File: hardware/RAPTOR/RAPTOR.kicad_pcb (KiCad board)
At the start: 2 copper layers, 68.6 x 53.3 mm, 12 parts, among them P1 Power, P2 Analog, P3 Digital, P4 Digital, P5 CONN_01X01, P6 CONN_01X01, P7 CONN_01X01, P8 CONN_01X01

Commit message: add net + pcb files
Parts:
- moved REF** 86.4 mm to (114.8, 109.9), turned to 90 degrees
- moved REF** 85.2 mm to (114.8, 87.0), turned to 90 degrees
- moved REF** 58.8 mm to (172.0, 107.3), turned to 270 degrees
- moved REF** 49.7 mm to (172.0, 84.5), turned to 270 degrees

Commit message: put stuff on pcb thing
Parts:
- removed REF**: BNO055, RAPTOR_footprints:BNO055
- removed REF**: OpenLog, RAPTOR_footprints:OpenLog
- removed REF**: BMP280, RAPTOR_footprints:BMP280
- removed REF**: Adafruit GPS, RAPTOR_footprints:AdafruitGPS
- added BZ1: Buzzer, Buzzer_Beeper:Buzzer_12x9.5RM7.6, F.Cu at (126.2, 88.3)
- added D8: DIODE-1N4148, Silicon-Custom:DIODE-1N4148, F.Cu at (179.6, 38.7)
- added D9: DIODE-1N4148, Silicon-Custom:DIODE-1N4148, F.Cu at (199.6, 59.0)
- added J1: SOLC_CONN, Connectors:1X02, F.Cu at (257.0, 42.5)
- added J10: EXT_LED3, Connectors:1X02, F.Cu at (229.1, 46.4)
- added J11: SRVOL_CONN, Connectors:1X03, F.Cu at (150.4, 41.3)
- added J12: SRVOR_CONN, Connectors:1X03, F.Cu at (210.1, 75.6)
- added J13: HOTWIRE_CONN, Connectors:1X02, F.Cu at (196.1, 40.0)
- added J14: RBF_CONN, Connectors:1X03, F.Cu at (165.6, 48.9)
- added J15: EEPROM_BTN_CONN, Connectors:1X02, F.Cu at (216.4, 45.1)
- added J16: SOLC_SW_CONN, Connectors:1X03, F.Cu at (232.9, 76.8)
- added J17: SOLP_SW_CONN, Connectors:1X03, F.Cu at (177.0, 57.8)
- added J2: SOLP_CONN, Connectors:1X02, F.Cu at (216.4, 19.7)
- added J4: CONN_LED_FIX, Connectors:1X02, F.Cu at (218.9, 65.4)
- added J5: CONN_SOLP_LED, Connectors:1X02, F.Cu at (222.8, 55.2)
- added J6: CONN_SOLC_LED, Connectors:1X02, F.Cu at (248.2, 73.0)
- added J7: EXT_LED0, Connectors:1X02, F.Cu at (259.6, 66.7)
- added J8: EXT_LED1, Connectors:1X02, F.Cu at (221.5, 84.5)
- added J9: EXT_LED2, Connectors:1X02, F.Cu at (229.1, 59.1)
- added Q1: MOSFET-NCH-2N7002PW, Silicon-Standard:TO-92, F.Cu at (210.1, 33.7)
- added Q2: MOSFET-NCH-2N7002PW, Silicon-Standard:TO-92, F.Cu at (246.9, 32.4)
- added Q3: MOSFET-NCH-2N7002PW, Silicon-Standard:TO-92, F.Cu at (236.7, 67.9)
- added Q4: MOSFET-NCH-2N7002PW, Silicon-Standard:TO-92, F.Cu at (227.8, 18.4)
- added Q5: MOSFET-NCH-2N7002PW, Silicon-Standard:TO-92, F.Cu at (250.7, 54.0)
- added R1: 20OHM-0603-1_10W-1%, Resistor_THT:R_Axial_DIN0204_L3.6mm_D1.6mm_P5.08mm_Horizontal, F.Cu at (238.0, 23.5)
- added R2: 100OHM-0603-1_10W-1%, Resistor_THT:R_Axial_DIN0204_L3.6mm_D1.6mm_P5.08mm_Horizontal, F.Cu at (271.0, 48.9)
- added R3: 100OHM-0603-1_10W-1%, Resistor_THT:R_Axial_DIN0204_L3.6mm_D1.6mm_P5.08mm_Horizontal, F.Cu at (268.5, 31.1)
- added R4: 100OHM-0603-1_10W-1%, Resistor_THT:R_Axial_DIN0204_L3.6mm_D1.6mm_P5.08mm_Horizontal, F.Cu at (268.5, 78.1)
- added R5: 4.7KOHM-0603-1_10W-1%, Resistor_THT:R_Axial_DIN0204_L3.6mm_D1.6mm_P5.08mm_Horizontal, F.Cu at (257.0, 15.9)
- added R6: 4.7KOHM-0603-1_10W-1%, Resistor_THT:R_Axial_DIN0204_L3.6mm_D1.6mm_P5.08mm_Horizontal, F.Cu at (248.2, 87.0)
- added R7: 4.7KOHM-0603-1_10W-1%, Resistor_THT:R_Axial_DIN0204_L3.6mm_D1.6mm_P5.08mm_Horizontal, F.Cu at (205.0, 50.2)
- added R8: 4.7KOHM-0603-1_10W-1%, Resistor_THT:R_Axial_DIN0204_L3.6mm_D1.6mm_P5.08mm_Horizontal, F.Cu at (192.3, 32.4)
- added U1: BMP280 Breakout, RAPTOR_footprints:BMP280, F.Cu at (154.2, 90.8)
- added U2: BNO055 Breakout, RAPTOR_footprints:BNO055, F.Cu at (137.7, 120.0)
- added U3: OpenLog, RAPTOR_footprints:OpenLog, F.Cu at (113.5, 89.5)
- added U4: AdafruitGPS, RAPTOR_footprints:AdafruitGPS, F.Cu at (175.8, 103.5)
- added U5: U3V12F12, RAPTOR_footprints:U3V12F12, F.Cu at (112.3, 109.9)
- added U6: D24V550F5, RAPTOR_footprints:D24v50f5_Reg, F.Cu at (113.5, 123.8)
- moved P8 2.84 mm to (175.8, 88.3)
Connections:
- P2 pad 1: /A0 -> (no net)
- P2 pad 2: /A1 -> (no net)
- P2 pad 3: /A2 -> (no net)
- P2 pad 4: /A3 -> (no net)
- P2 pad 5: /A4(SDA) -> (no net)
- P2 pad 6: /A5(SCL) -> (no net)
- P3 pad 1: /A5(SCL) -> (no net)
- P3 pad 10: /8 -> (no net)
- P3 pad 2: /A4(SDA) -> (no net)
- P3 pad 3: /AREF -> (no net)
- P3 pad 4: GND -> (no net)
- P3 pad 5: /13(SCK) -> (no net)
- P3 pad 6: /12(MISO) -> (no net)
- P3 pad 7: /11(**/MOSI) -> (no net)
- P3 pad 8: /10(**/SS) -> /SOLC_DTA
- P3 pad 9: /9(**) -> (no net)
- P4 pad 1: /7 -> (no net)
- P4 pad 2: /6(**) -> /GPS_RX
- P4 pad 3: /5(**) -> (no net)
- P4 pad 4: /4 -> /HOTWIRE
- P4 pad 5: /3(**) -> (no net)
- P4 pad 6: /2 -> (no net)
- P4 pad 7: /1(Tx) -> /EEPROM_BTN
- P4 pad 8: /0(Rx) -> (no net)

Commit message: extend board
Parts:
- moved U4 39.4 mm to (215.1, 103.0)
- moved P8 1.98 mm to (177.0, 89.8)
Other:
- board size 68.6 x 53.3 mm -> 88.9 x 53.3 mm
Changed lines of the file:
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@@
   (general
     (thickness 1.6)
-    (drawings 27)
+    (drawings 24)
     (tracks 0)
     (zones 0)
@@
   )
   (module Socket_Arduino_Uno:Arduino_1pin locked (layer F.Cu)
-    (at 175.768 88.265)
+    (at 177.038 89.789)
     (descr "module 1 pin (ou trou mecanique de percage)")
     (tags DEV)
@@
   )
   (module RAPTOR_footprints:AdafruitGPS (layer F.Cu)
-    (at 175.768 103.505 270)
+    (at 215.138 102.997 270)
     (descr "A footprint for the Adafruit GPS Breakout Board")
     (fp_text reference U4 (at 0 3.81 270) (layer F.SilkS)
@@
     )
   )
+  (gr_line (start 199.898 73.025) (end 175.514 73.025) (layer Edge.Cuts) (width 0.15))
+  (gr_line (start 199.898 126.365) (end 199.898 73.025) (layer Edge.Cuts) (width 0.15))
+  (gr_line (start 177.038 126.365) (end 199.898 126.365) (layer Edge.Cuts) (width 0.15))
   (gr_text 1 (at 138.938 121.285 90) (layer F.SilkS)
     (effects (font (size 1 1) (thickness 0.15)))
@@
   (gr_line (start 114.427 74.93) (end 120.269 74.93) (angle 90) (layer Dwgs.User) (width 0.15))
   (gr_line (start 120.523 93.98) (end 104.648 93.98) (angle 90) (layer Dwgs.User) (width 0.15))
-  (gr_line (start 177.038 74.549) (end 175.514 73.025) (angle 90) (layer Edge.Cuts) (width 0.15))
-  (gr_line (start 177.038 85.979) (end 177.038 74.549) (angle 90) (layer Edge.Cuts) (width 0.15))
-  (gr_line (start 179.578 88.519) (end 177.038 85.979) (angle 90) (layer Edge.Cuts) (width 0.15))
-  (gr_line (start 179.578 121.285) (end 179.578 88.519) (angle 90) (layer Edge.Cuts) (width 0.15))
-  (gr_line (start 177.038 123.825) (end 179.578 121.285) (angle 90) (layer Edge.Cuts) (width 0.15))
-  (gr_line (start 177.038 126.365) (end 177.038 123.825) (angle 90) (layer Edge.Cuts) (width 0.15))
   (gr_line (start 110.998 126.365) (end 177.038 126.365) (angle 90) (layer Edge.Cuts) (width 0.15))
   (gr_line (start 110.998 73.025) (end 110.998 126.365) (angle 90) (layer Edge.Cuts) (width 0.15))

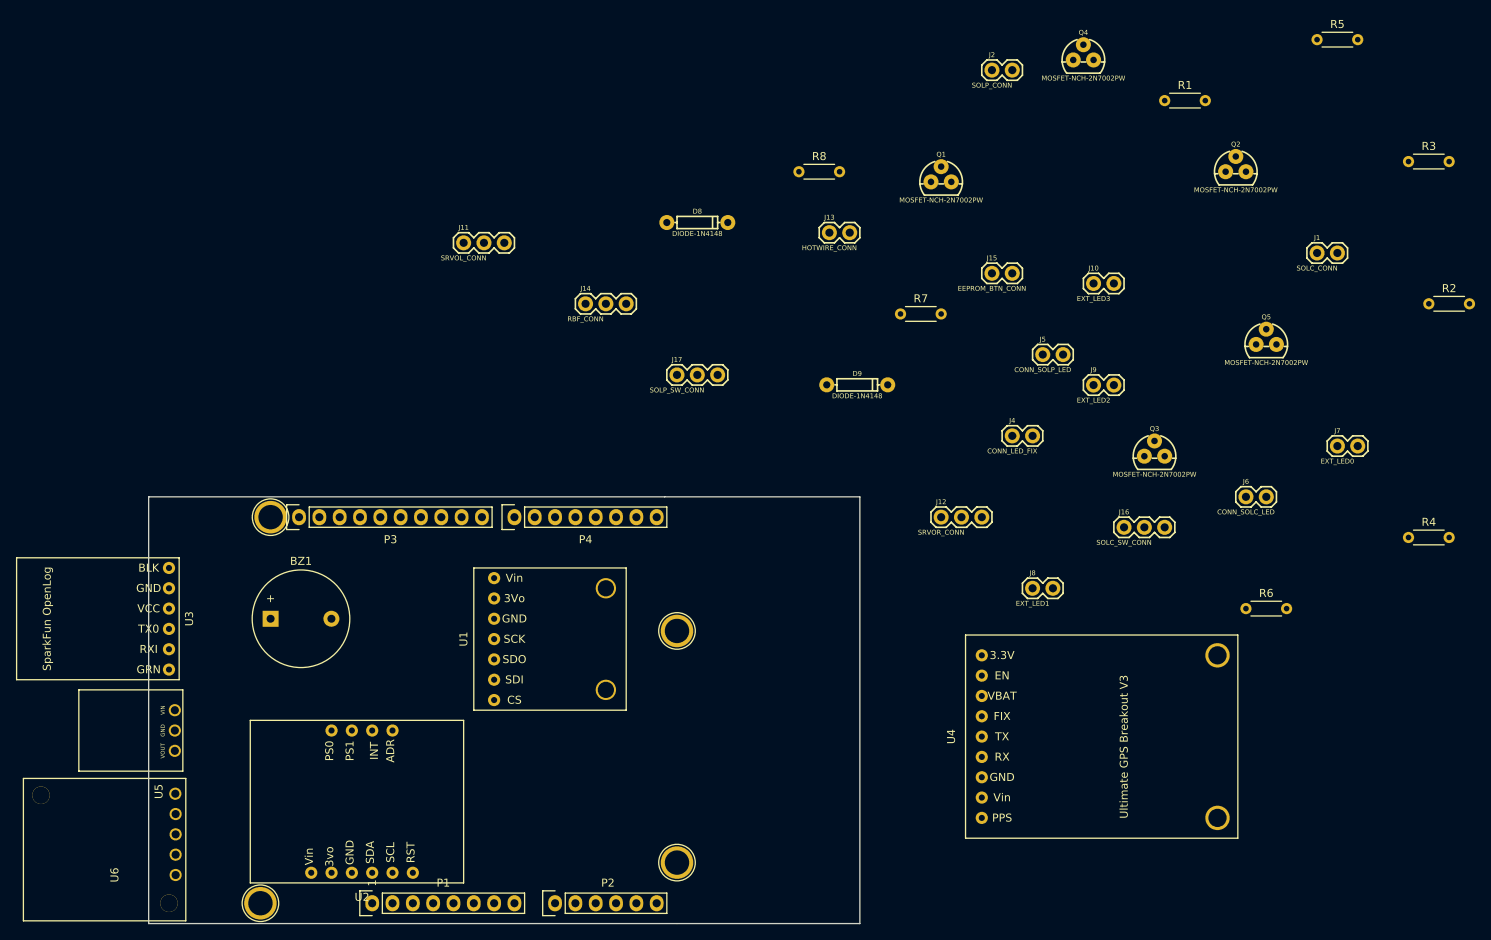
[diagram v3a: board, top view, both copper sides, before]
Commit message: Fitted parts
Placed all the compnents on the actual PCB not just off to the side
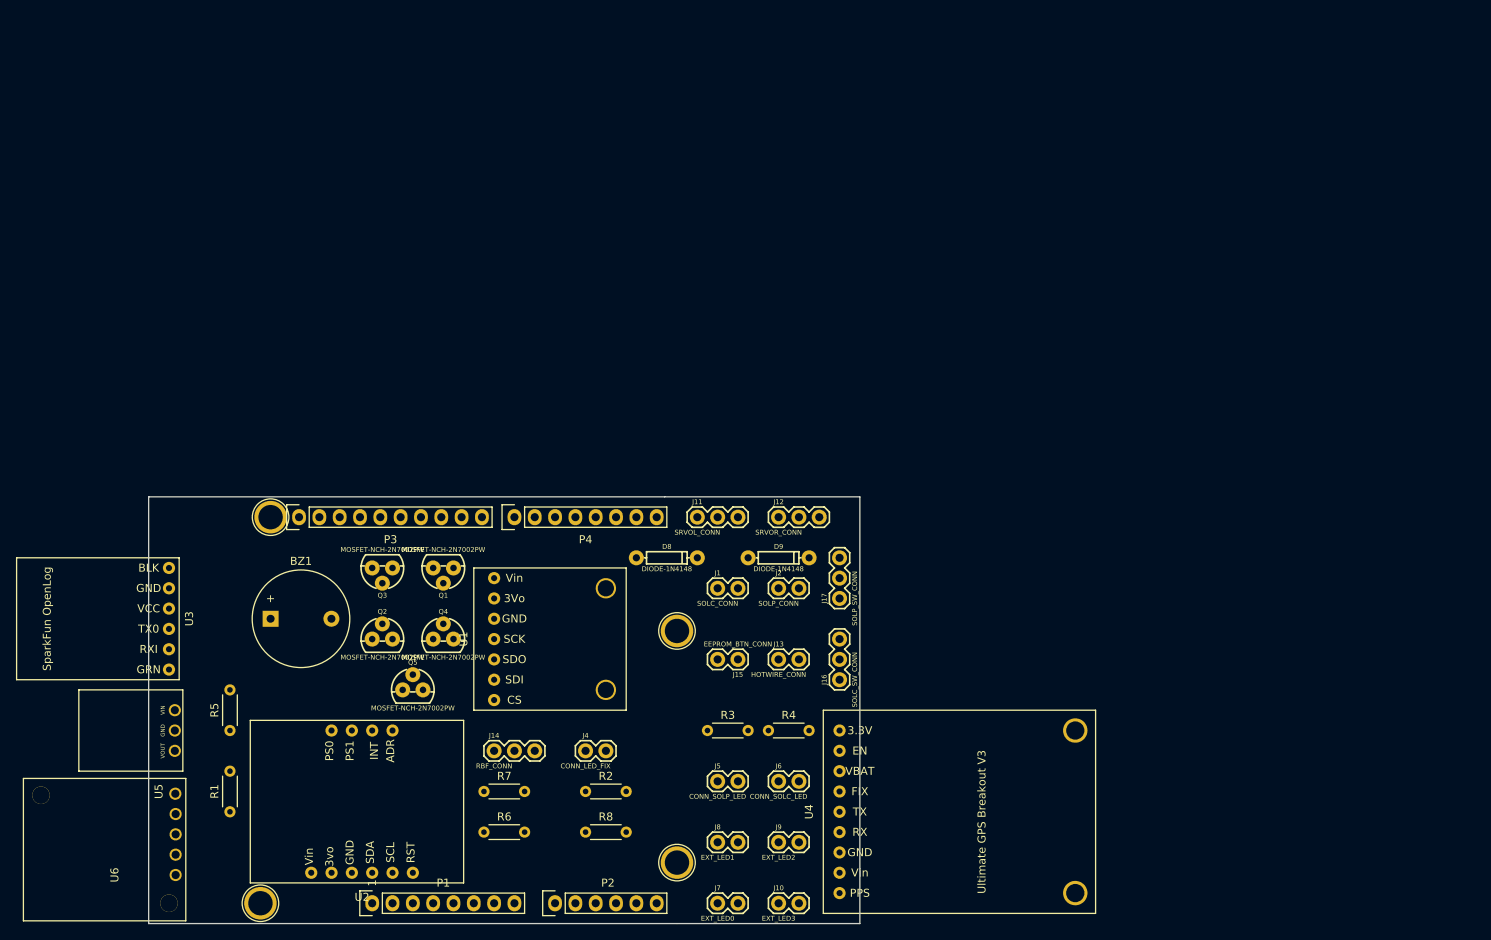
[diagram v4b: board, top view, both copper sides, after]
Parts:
- moved R5 161.0 mm to (121.2, 102.2), turned to 90 degrees
- moved R1 146.8 mm to (121.2, 112.4), turned to 90 degrees
- moved R2 121.8 mm to (165.6, 109.9)
- moved Q2 121.6 mm to (140.2, 90.8)
- moved Q5 115.1 mm to (144.0, 97.2)
- moved R3 112.9 mm to (180.8, 102.2)
- moved Q4 107.9 mm to (147.8, 90.8)
- moved R6 99.3 mm to (152.9, 114.9)
- moved Q3 97.5 mm to (140.2, 81.9), turned to 180 degrees
- moved J7 96.3 mm to (182.1, 123.8)
- moved J10 86.9 mm to (189.7, 123.8)
- moved R8 86.8 mm to (165.6, 114.9)
- moved J1 85.9 mm to (182.1, 84.5)
- moved R4 83.6 mm to (188.5, 102.2)
- moved R7 79.2 mm to (152.9, 109.9)
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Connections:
- net /SOLC_LED renamed /LEDC_DTA
- net /SOLP_LED renamed /LEDP_DTA

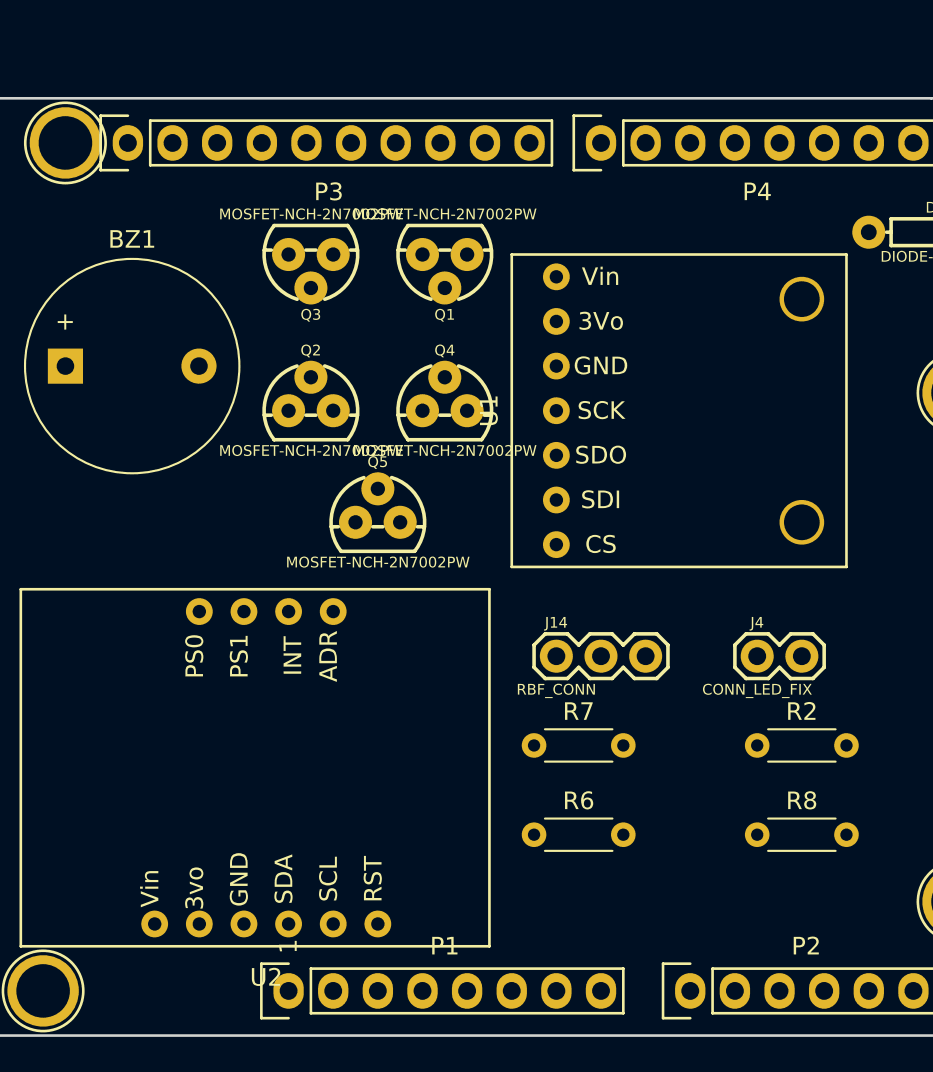
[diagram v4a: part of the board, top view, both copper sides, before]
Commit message: PCB Error Fixing
Changed footprints and symbols to be more accurate
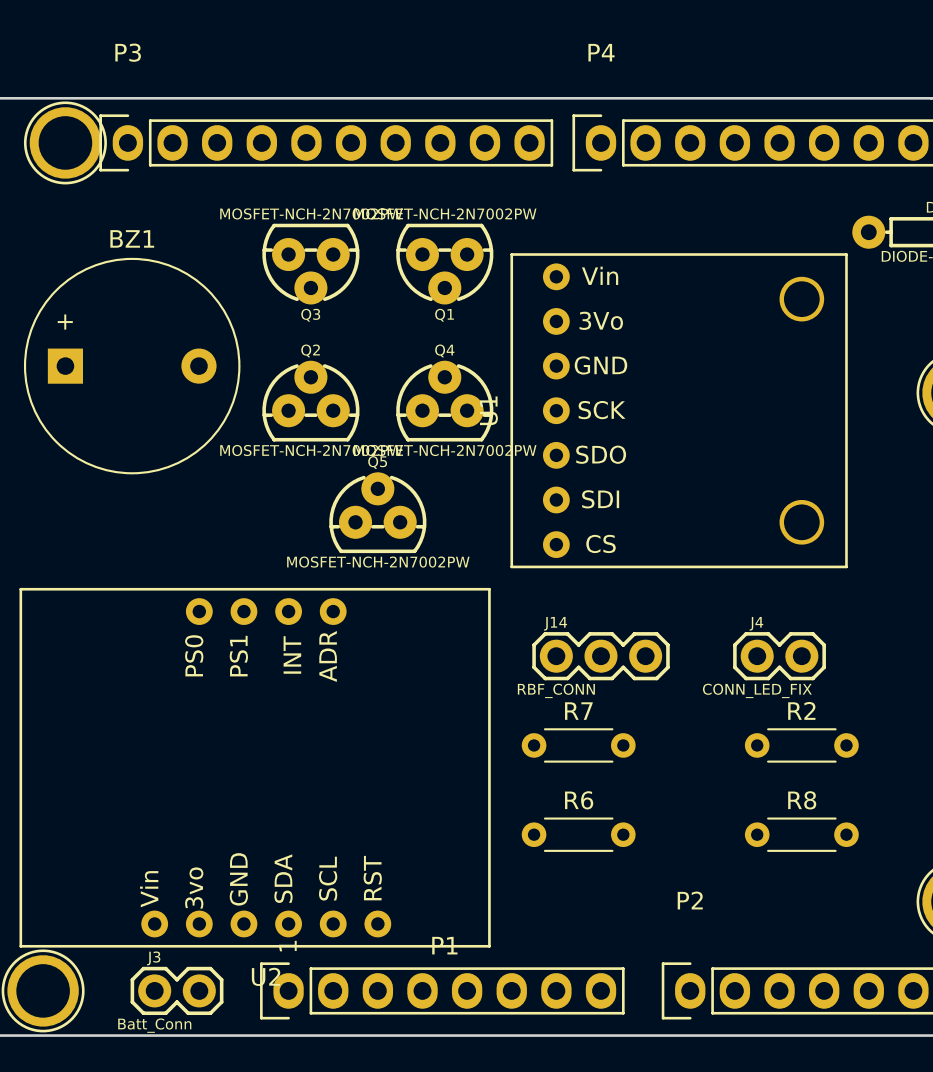
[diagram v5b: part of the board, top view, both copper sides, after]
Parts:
- added J3: Batt_Conn, RAPTOR_footprints:2_Pin_Connector, F.Cu at (131.3, 123.8)
- P2: footprint Socket_Arduino_Uno:Socket_Strip_Arduino_1x06 -> RAPTOR_footprints:Arduino_Analog_06
- P3: footprint Socket_Arduino_Uno:Socket_Strip_Arduino_1x10 -> RAPTOR_footprints:Arduino_x10_Digital
- P4: footprint Socket_Arduino_Uno:Socket_Strip_Arduino_1x08 -> RAPTOR_footprints:Arduino_x08_Digital
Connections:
- P1 pad 8: /Vin -> +7.5V
- U5 pad 1: +7.5V -> +12V
- U5 pad 3: +12V -> +7.5V
- U6 pad 1: +7.5V -> Net-(U6-Pad1)
- U6 pad 2: GND -> +7.5V
- U6 pad 3: +5V -> GND
- U6 pad 4: (no net) -> GND
- U6 pad 5: (no net) -> +5V

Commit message: Test of mergy bois
^^^^
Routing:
- net +5V: track 0.00 -> 15.2 mm
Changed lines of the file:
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@@
     (thickness 1.6)
     (drawings 24)
-    (tracks 0)
+    (tracks 2)
     (zones 0)
     (modules 47)
@@
   (gr_line (start 120.523 82.55) (end 120.523 93.98) (angle 90) (layer Dwgs.User) (width 0.15))
   (gr_line (start 104.648 82.55) (end 120.523 82.55) (angle 90) (layer Dwgs.User) (width 0.15))
+  (segment (start 184.658 93.345) (end 184.658 95.885) (width 0.25) (layer F.Cu) (net 3))
+  (segment (start 184.658 95.885) (end 197.358 95.885) (width 0.25) (layer F.Cu) (net 3))
 )
